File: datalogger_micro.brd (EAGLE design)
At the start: 32 x 40.6 mm, 46 parts, among them IC1 DS3231/SO, IC3 LD117AS33TR, M0 PAT, M1 PAT, Q4 IRLML5203

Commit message: VERSION 0.95
finalized Version 0.95, to be printed
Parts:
- moved C6 12.1 mm to (24.4, 40.0), turned to 90 degrees
- moved Q4 4.55 mm to (30.0, 40.0), turned to 0 degrees
- moved C3 3.59 mm to (32.1, 33.5)
- moved R8 3.18 mm to (26.0, 40.0), turned to 90 degrees
- moved R16 2.90 mm to (20.6, 27.3)
- moved POWER 2.67 mm to (32.3, 27.4), turned to 0 degrees
- moved IC3 1.98 mm to (27.2, 33.7), turned to 180 degrees
- moved C8 1.91 mm to (22.0, 27.3), turned to 270 degrees
- moved R6 1.67 mm to (33.7, 10.5)
- moved D3 1.52 mm to (33.8, 14.0)
- moved R11 1.42 mm to (35.1, 10.4)
- moved LED1 1.40 mm to (35.2, 14.0)
- moved R17 1.20 mm to (21.1, 29.5)
- moved R7 1.17 mm to (23.2, 21.5)
- moved C1 1.15 mm to (16.5, 14.0)
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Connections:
- net D10 renamed FLASH_CE
- net D3 renamed INT1
- net D7 renamed RTC_VCC
- net D8 renamed RTC_INT
- removed net A0: ATMEGA328P.23, Q2.2, R5.1
- removed net A1: ATMEGA328P.24, Q3.2, R10.1
- removed net A2: ATMEGA328P.25, R12.2, R14.1, VD2.2
- removed net A3: ATMEGA328P.26, R13.2, R15.1, VD3.2
- removed net D2: ATMEGA328P.32, IC1.4
- removed net D4: ATMEGA328P.2, R6.1
- removed net D5: ATMEGA328P.9, Q4.1, R8.1
- removed net D6: ATMEGA328P.10
- removed net D9: ATMEGA328P.13
- new net INT0: ATMEGA328P.32
- new net LED1: ATMEGA328P.9, R6.1
- new net RTC_RST: ATMEGA328P.24, IC1.4
- new net SOIL1: ATMEGA328P.22, Q2.2, R5.1
- new net SOIL2: ATMEGA328P.25, Q3.2, R10.1
- new net VCC/ST_ON: ATMEGA328P.13, Q4.1, R8.1
- new net VDIV1: ATMEGA328P.23, R13.2, R15.1, VD3.2
- new net VDIV2: ATMEGA328P.26, R12.2, R14.1, VD2.2
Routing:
- net SOIL1: track 0.00 -> 36.9 mm, vias 0 -> 4
- net VBAT: track 132.0 -> 168.4 mm, vias 4 -> 5
- net A3: track 36.4 -> 0.00 mm, vias 2 -> 0
- net A0: track 36.3 -> 0.00 mm, vias 4 -> 0
- net VCC/ST_ON: track 0.00 -> 35.9 mm, vias 0 -> 2
- net VDIV1: track 0.00 -> 35.2 mm, vias 0 -> 2
- net A2: track 33.1 -> 0.00 mm, vias 2 -> 0
- net VDIV2: track 0.00 -> 30.8 mm, vias 0 -> 2
- net D4: track 29.6 -> 0.00 mm, vias 2 -> 0
- net D5: track 28.1 -> 0.00 mm, vias 2 -> 0
- net A1: track 25.3 -> 0.00 mm, vias 2 -> 0
- net D2: track 24.8 -> 0.00 mm, vias 2 -> 0
- net SOIL2: track 0.00 -> 23.4 mm, vias 0 -> 2
- net LED1: track 0.00 -> 20.4 mm, vias 0 -> 2
- net GND: track 17.5 -> 2.96 mm, vias 13 -> 19
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
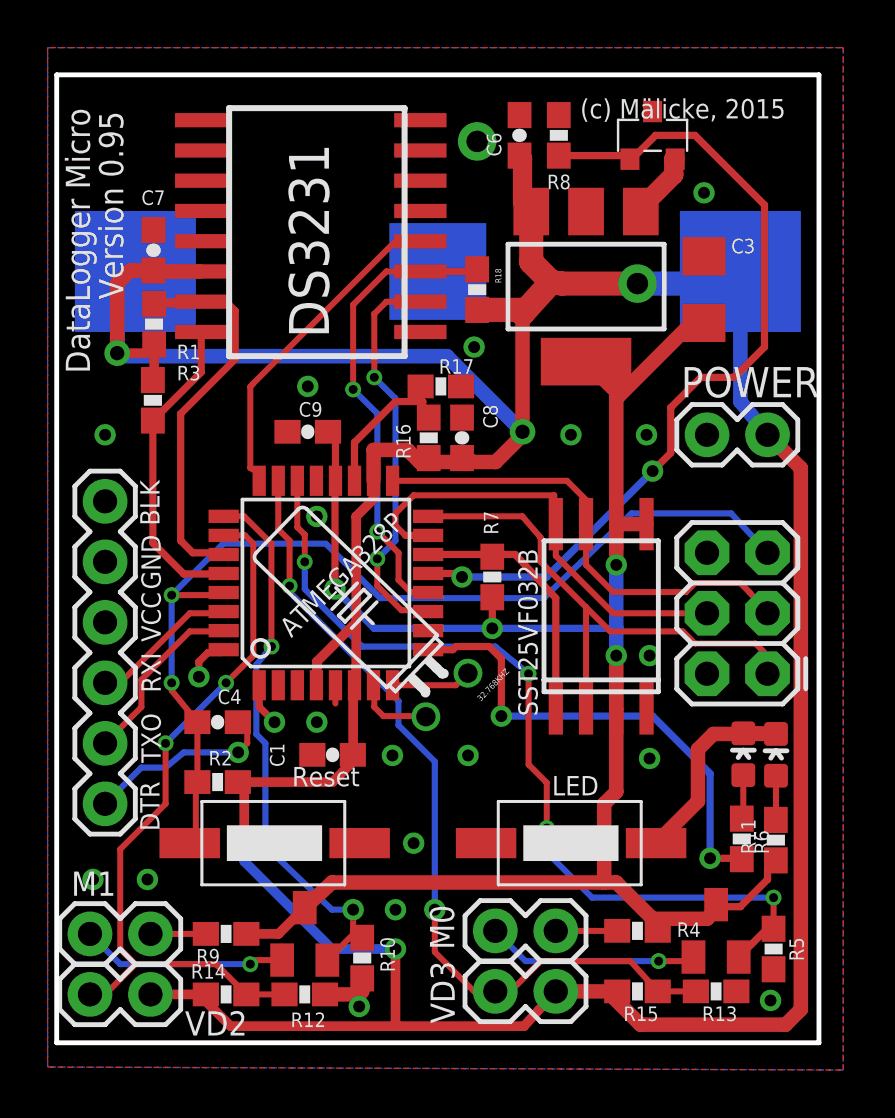
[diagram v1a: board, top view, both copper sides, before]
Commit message: bugfix
removed a uneccessary connection
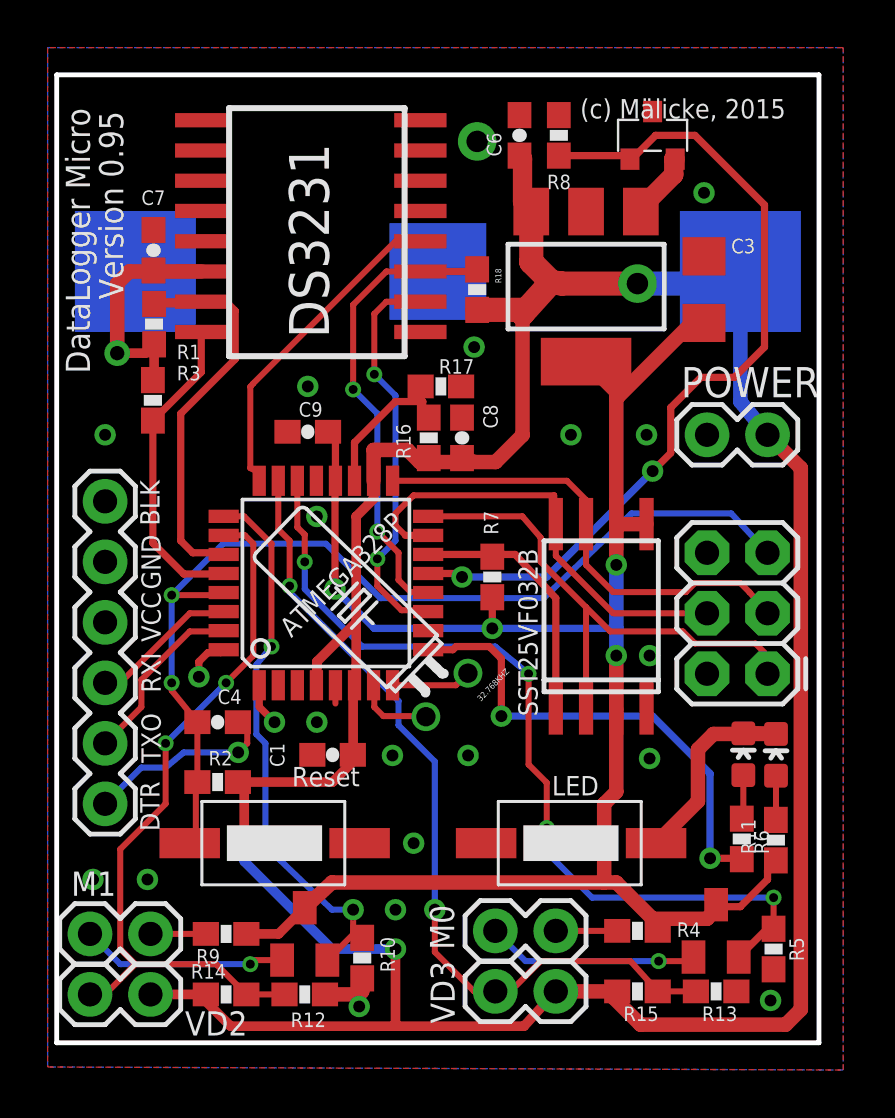
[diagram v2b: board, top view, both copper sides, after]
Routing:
- net VBAT: track 168.4 -> 143.9 mm, vias 5 -> 4
- net SOIL2: track 23.4 -> 22.9 mm

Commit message: VERSION 0.95 final
final printed Version 0.95 to be published
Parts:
- removed C9: 0.1uF, SparkFun:0603-CAP
- removed IC3: LD117AS33TR, v-reg:SOT223
- removed Q4: IRLML5203, transistor-power:MICRO3
- removed U$5: DRUCKTASTER-1PIN, Edu Logger Basic Components:DRUCKTASTER-1PIN
- removed VD3: PAT, SparkFun:1X02
- added C2: 0.1uF, SparkFun:0603-CAP
- added IC2: LD117AS33TR, v-reg:SOT223
- added Q1: (no value), semicon-smd-ipc:SOT23
- added U$3: SST25VF032B, SST25:SO-08
- added VD1: PAT, SparkFun:1X02
- C3: value 10uF -> 0.1uF; device SparkFun:1206 -> SparkFun:0603-CAP
- C7: value 0.1uF -> 10uF; device SparkFun:0603-CAP -> SparkFun:1206
- Q2: value (none) -> IRLML5203; device semicon-smd-ipc:SOT23 -> transistor-power:MICRO3
- R10: value 100 -> 10k
- R11: value 470 -> 100K
- R12: value VAR -> 100k
- R13, R17: value VAR -> 100
- R16: value VAR -> 470
- R18: value 10k -> 470
- R5, R9: value 100 -> VAR
- R6: value 470 -> VAR
- R7: value 100K -> 100
- R8: value 100k -> VAR
- U$2: value SST25VF032B -> DRUCKTASTER-1PIN; device SST25:SO-08 -> Edu Logger Basic Components:DRUCKTASTER-1PIN
- moved R12 37.7 mm to (26.4, 40.0), turned to 90 degrees
- moved Q2 33.5 mm to (30.4, 40.0)
- moved R10 28.5 mm to (22.7, 33.5)
- moved R17 27.4 mm to (35.1, 5.84), turned to 270 degrees
- moved R18 26.3 mm to (35.1, 10.4)
- moved R9 24.7 mm to (21.1, 29.5)
- moved C7 23.9 mm to (32.9, 33.5), turned to 90 degrees
- moved R5 23.1 mm to (12.1, 3.94), turned to 180 degrees
- moved C1 22.6 mm to (8.76, 35.2), turned to 270 degrees
- moved R16 21.4 mm to (33.7, 10.5)
- moved R6 19.5 mm to (15.4, 3.94), turned to 180 degrees
- moved C3 17.7 mm to (15.5, 27.6), turned to 0 degrees
- moved Q3 17.3 mm to (32.6, 6.60)
- moved R14 17.3 mm to (29.3, 4.06)
- moved R4 17.3 mm to (12.1, 6.48)
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- renumbered C8 to C5, D3 to D1, M0 to M2, U$4 to U$100
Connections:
- net A5: now also R2.1; no longer R3.1
- net A6: now also R8.2, R9.2; no longer R16.2, R17.2
- net DTR: now also C2.2; no longer C4.2
- net FLASH_CE: now also R11.2, U$3.1; no longer R7.2, U$2.1
- net GND: now also C3.1, C4.1, C7.2, Q2.3, R12.2, R15.1, R17.2, R6.1, R7.2, R9.1, U$2.P$2, U$3.4; no longer C3.2, C7.1, C9.1, Q4.3, R10.2, R12.1, R13.1, R17.1, R5.2, R8.2, U$2.4, U$5.P$2
- net GNDA: now also U$2.P$1; no longer U$5.P$1
- net LED1: now also R16.1; no longer R6.1
- net MISO: now also U$3.2; no longer U$2.2
- net MOSI: now also U$3.8; no longer U$2.8
- net N$1: now also IC2.1, Q2.2; no longer IC3.1, Q4.2
- net N$4: now also R18.1; no longer R11.1
- net N$5: now also Q1.1; no longer Q3.1
- net N$6: now also Q3.1; no longer Q2.1
- net N$7: now also R16.2; no longer R6.2
- net N$8: now also R4.2; no longer R9.2
- net N$9: now also R13.2; no longer R4.2
- net RESET: now also C2.1, R3.1; no longer C4.1, R2.1
- net RTC_INT: now also R10.1; no longer R18.1
- net SCK: now also U$3.7; no longer U$2.7
- net SOIL1: now also Q3.2, R17.1; no longer Q2.2, R5.1
- net SOIL2: now also Q1.2, R7.1; no longer Q3.2, R10.1
- net VBAT: now also C4.2, IC2.3, R10.2, R5.2, R8.1, VD1.1; no longer C7.2, IC3.3, R15.2, R16.1, R18.2, VD3.1
- net VCC-ST: now also C3.2, C7.1, IC2.4, Q1.3, R11.1, R13.1, R18.2, U$3.3, U$3.5, U$3.6; no longer C3.1, C9.2, IC3.4, Q2.3, R11.2, R7.1, R9.1, U$2.3, U$2.5, U$2.6
- net VCC/ST_ON: now also Q2.1, R12.1; no longer Q4.1, R8.1
- net VDIV1: now also R14.1, R15.2, VD2.2; no longer R13.2, R15.1, VD3.2
- net VDIV2: now also R5.1, R6.2, VD1.2; no longer R12.2, R14.1, VD2.2
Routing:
- net A5: track 13.2 -> 14.7 mm
- net VCC-ST: track 76.0 -> 77.0 mm
- net FLASH_CE: track 11.3 -> 10.3 mm
- net A4: track 18.2 -> 18.7 mm
- net SOIL2: track 22.9 -> 23.4 mm
- net VBAT: track 143.9 -> 144.4 mm
